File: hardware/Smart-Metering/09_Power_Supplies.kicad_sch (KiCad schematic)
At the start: 36 parts, among them J901 BATTERY_1S, SW901 POWER, U901 BQ24074RGT, U902 TPS63001, U903 TPS61089

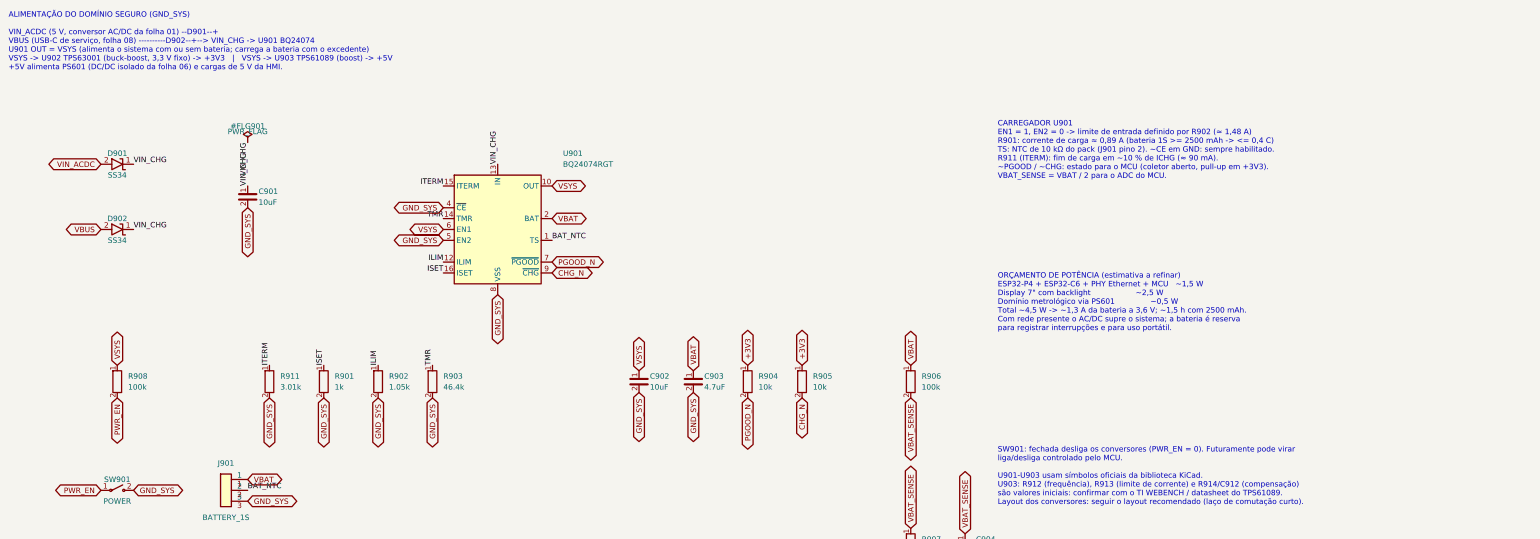
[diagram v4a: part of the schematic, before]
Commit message: Troca o carregador linear BQ24074 pelo chaveado BQ25895
O BQ24074 limitava a entrada a 1,48 A e, com o sistema consumindo cerca
de 5,2 W, sobravam só ~0,3 A para carregar a bateria (mais de 8 h).

09_Power_Supplies:
- U901 BQ25895RTW (símbolo oficial): carregador chaveado com power path
  NVDC; limite de entrada de 2,0 A por R902 (180 Ω), o máximo do
  IRM-10-5; carga de ~0,85 A com a tela ligada;
- D+/D- unidos para detecção como carregador dedicado (DCP);
- divisor do NTC a partir de REGN, L903 2,2 uH, bootstrap, REGN, PMID,
  SYS e BAT conforme o datasheet;
- I2C, ~INT e STAT para o MCU; D901/D902 passam a SS54 (SMC);
- PWR_FLAG em VSYS (pino SYS é passivo no símbolo oficial).

05_Metrology_MCU: PC2 = CHG_INT_N, PB6/PB7 = I2C1 para o carregador.
Documentação de revisão e README atualizados.

Co-Authored-By: Claude Opus 5.5 <noreply@anthropic.com>
Claude-Session: https://claude.ai/code/session_012B8cVkhtjf3eg98UdpNCpf
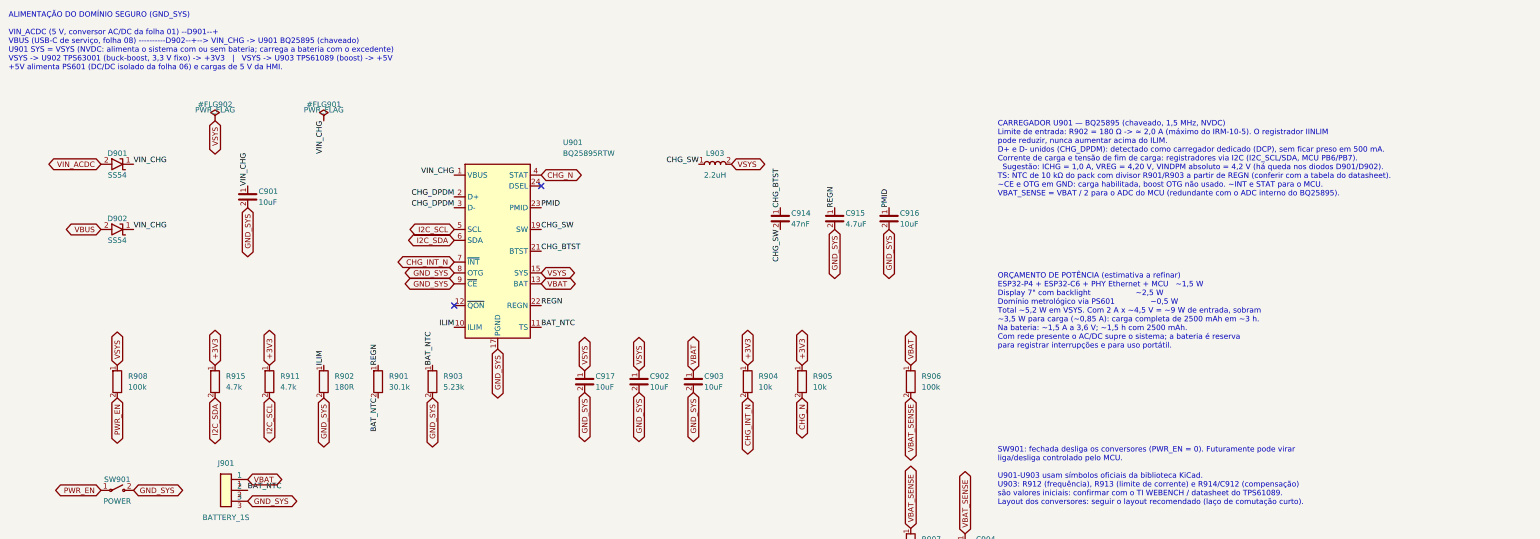
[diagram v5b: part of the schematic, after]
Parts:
- removed U901: BQ24074RGT, Package_DFN_QFN:VQFN-16-1EP_3x3mm_P0.5mm_EP1.6x1.6mm, symbol Battery_Management:BQ24074RGT
- added C914: 47nF, Capacitor_SMD:C_0603_1608Metric, symbol SmartMetering:C_Vert
- added C915: 4.7uF, Capacitor_SMD:C_0805_2012Metric, symbol SmartMetering:C_Vert
- added C916, C917: 10uF, Capacitor_SMD:C_0805_2012Metric, symbol SmartMetering:C_Vert
- added L903: 2.2uH, Inductor_SMD:L_Bourns_SRP7028A_7.3x6.6mm, symbol SmartMetering:L_Horiz
- added R915: 4.7k, Resistor_SMD:R_0603_1608Metric, symbol SmartMetering:R_Vert
- added U901: BQ25895RTW, Package_DFN_QFN:Texas_RTW_WQFN-24-1EP_4x4mm_P0.5mm_EP2.7x2.7mm_ThermalVias, symbol Battery_Management:BQ25895RTW
- C903: value 4.7uF -> 10uF
- D901, D902: value SS34 -> SS54; footprint Diode_SMD:D_SMA -> Diode_SMD:D_SMC
- R901: value 1k -> 30.1k
- R902: value 1.05k -> 180R
- R903: value 46.4k -> 5.23k
- R911: value 3.01k -> 4.7k
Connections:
- net ITERM is gone; now on net +3V3: R911.1
- net TMR is gone; now on net BAT_NTC: R903.1
- net +3V3: now also R915.1
- net BAT_NTC: now also R901.2, U901.11 (TS)
- net CHG_N: now also U901.4 (STAT)
- net GND_SYS: now also C915.2, C916.2, C917.2, U901.17 (PGND), U901.18 (PGND), U901.25 (PGND), U901.8 (OTG), U901.9 (~{CE}); no longer R901.2, R911.2
- net ILIM: now also U901.10 (ILIM)
- net VBAT: now also U901.13 (BAT), U901.14 (BAT)
- net VIN_CHG: now also U901.1 (VBUS)
- net VSYS: now also C917.1, L903.2, U901.15 (SYS), U901.16 (SYS)
- net ISET renamed REGN
- net REGN: now also C915.1, U901.22 (REGN)
- net PGOOD_N renamed CHG_INT_N
- net CHG_INT_N: now also U901.7 (~{INT})
- new net CHG_BTST: C914.1, U901.21 (BTST)
- new net CHG_DPDM: U901.2 (D+), U901.3 (D-)
- new net CHG_SW: C914.2, L903.1, U901.19 (SW), U901.20 (SW)
- new net I2C_SCL: R911.2, U901.5 (SCL)
- new net I2C_SDA: R915.2, U901.6 (SDA)
- new net PMID: C916.1, U901.23 (PMID)
- no-connect marks 0 -> 2
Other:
- note added: "ALIMENTAÇÃO DO DOMÍNIO SEGURO (GND_SYS) VIN_ACDC (5 V, conversor AC/DC da folha 01) --D901--+ VBUS (USB-C de serviço, folha 08) ----------D902--+--> VIN_CHG -> U901 BQ25895 (chaveado) U901 SYS = VSYS (NVDC: alimenta o sistema com ou sem bateria; carrega a bateria com o excedente) VSYS -> U902 TPS63001 (buck-boost, 3,3 V fixo) -> +3V3 | VSYS -> U903 TPS61089 (boost) -> +5V +5V alimenta PS601 (DC/D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"
- note added: "CARREGADOR U901 — BQ25895 (chaveado, 1,5 MHz, NVDC) Limite de entrada: R902 = 180 Ω -> ≈ 2,0 A (máximo do IRM-10-5). O registrador IINLIM pode reduzir, nunca aumentar acima do ILIM. D+ e D- unidos (CHG_DPDM): detectado como carregador dedicado (DCP), sem ficar preso em 500 mA. Corrente de carga e tensão de fim de carga: registradores via I2C (I2C_SCL/SDA, MCU PB6/PB7). Sugestão: ICHG = 1,0 A, VRE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"
- note added: "ORÇAMENTO DE POTÊNCIA (estimativa a refinar) ESP32-P4 + ESP32-C6 + PHY Ethernet + MCU ~1,5 W Display 7" com backlight ~2,5 W Domínio metrológico via PS601 ~0,5 W Total ~5,2 W em VSYS. Com 2 A x ~4,5 V = ~9 W de entrada, sobram ~3,5 W para carga (~0,85 A): carga completa de 2500 mAh em ~3 h. Na bateria: ~1,5 A a 3,6 V; ~1,5 h com 2500 mAh. Com rede presente o AC/DC supre o sistema; a bateria é res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"
- note removed: "ALIMENTAÇÃO DO DOMÍNIO SEGURO (GND_SYS) VIN_ACDC (5 V, conversor AC/DC da folha 01) --D901--+ VBUS (USB-C de serviço, folha 08) ----------D902--+--> VIN_CHG -> U901 BQ24074 U901 OUT = VSYS (alimenta o sistema com ou sem bateria; carrega a bateria com o excedente) VSYS -> U902 TPS63001 (buck-boost, 3,3 V fixo) -> +3V3 | VSYS -> U903 TPS61089 (boost) -> +5V +5V alimenta PS601 (DC/DC isolado da folh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"
- note removed: "CARREGADOR U901 EN1 = 1, EN2 = 0 -> limite de entrada definido por R902 (≈ 1,48 A) R901: corrente de carga ≈ 0,89 A (bateria 1S >= 2500 mAh -> <= 0,4 C) TS: NTC de 10 kΩ do pack (J901 pino 2). ~CE em GND: sempre habilitado. R911 (ITERM): fim de carga em ~10 % de ICHG (≈ 90 mA). ~PGOOD / ~CHG: estado para o MCU (coletor aberto, pull-up em +3V3). VBAT_SENSE = VBAT / 2 para o ADC do MCU."
- note removed: "ORÇAMENTO DE POTÊNCIA (estimativa a refinar) ESP32-P4 + ESP32-C6 + PHY Ethernet + MCU ~1,5 W Display 7" com backlight ~2,5 W Domínio metrológico via PS601 ~0,5 W Total ~4,5 W -> ~1,3 A da bateria a 3,6 V; ~1,5 h com 2500 mAh. Com rede presente o AC/DC supre o sistema; a bateria é reserva para registrar interrupções e para uso portátil."

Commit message: Resolve as pendências da revisão do esquemático
P1  ADE9430: footprint VQFN-40 6x6 com EP de 4,15 mm, compatível com as
    variantes CP-40 de 6x6 mm (EP de 3,9 a 4,7 mm).
P2  Confirmado no datasheet: MISO solto com SS alto (pull-up de 100 kΩ)
    e NC1/NC2 em GND, como já estava.
P3  J301-J304: headers JST PH de 4 vias cabeados até conectores M8
    fêmea de painel (à prova de toque).
P4  PS601 -> U606 ADuM6000 (isoPower 5 kVrms, símbolo oficial).
P5  PS101 -> RAC20-05SK/277 (85-305 VAC, 120-430 VDC, 20 W); fusíveis
    T500mA, R101 3 W, C101 10 uF/450 V; entrada do BQ25895 a 3 A.
P7  TPS61089 -> TPS61022 (compensação interna, sem valores a ajustar).
P8  Placa EV alimentada pelos pinos 5 V do J1 (nota na folha 07).
P9  EEPROM de calibração 24LC64 no I2C1.
P10 Labels globais de uma só folha convertidos em locais.

Verificação: 223 componentes, nenhum pino solto, nenhuma net sem fonte,
nenhum conflito de saída, isolação íntegra, todos os footprints
existentes na biblioteca oficial do KiCad.

Co-Authored-By: Claude Opus 5.5 <noreply@anthropic.com>
Claude-Session: https://claude.ai/code/session_012B8cVkhtjf3eg98UdpNCpf
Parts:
- removed C912: 4.7nF, Capacitor_SMD:C_0603_1608Metric, symbol SmartMetering:C_Vert
- removed C913: 2.2uF, Capacitor_SMD:C_0603_1608Metric, symbol SmartMetering:C_Vert
- removed R912: 301k, Resistor_SMD:R_0603_1608Metric, symbol SmartMetering:R_Vert
- removed R913: 200k, Resistor_SMD:R_0603_1608Metric, symbol SmartMetering:R_Vert
- removed R914: 15k, Resistor_SMD:R_0603_1608Metric, symbol SmartMetering:R_Vert
- removed U903: TPS61089, Package_DFN_QFN:Texas_VQFN-RNR0011A-11, symbol Regulator_Switching:TPS61089
- added U903: TPS61022, Package_DFN_QFN:Texas_RWU0007A_VQFN-7_2x2mm_P0.5mm, symbol Converter_DCDC:TPS61022
- C908: value 10uF -> 22uF; footprint Capacitor_SMD:C_0805_2012Metric -> Capacitor_SMD:C_1206_3216Metric
- C911: value 100nF -> 22uF; footprint Capacitor_SMD:C_0603_1608Metric -> Capacitor_SMD:C_1206_3216Metric
- L902: value 2.2uH -> 1uH
- R902: value 180R -> 120R
- R909: value 316k -> 732k
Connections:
- net BOOT_5V is gone; now on net +5V: C911.1
- net +5V: now also U903.3 (VOUT)
- net FB_5V: now also U903.4 (FB)
- net GND_SYS: now also C911.2, U903.1 (GND)
- net PWR_EN: now also U903.5 (EN)
- net SW_5V: now also U903.2 (SW); no longer C911.2
- net VSYS: now also U903.6 (MODE), U903.7 (VIN)
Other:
- note added: "ALIMENTAÇÃO DO DOMÍNIO SEGURO (GND_SYS) VIN_ACDC (5 V, conversor AC/DC da folha 01) --D901--+ VBUS (USB-C de serviço, folha 08) ----------D902--+--> VIN_CHG -> U901 BQ25895 (chaveado) U901 SYS = VSYS (NVDC: alimenta o sistema com ou sem bateria; carrega a bateria com o excedente) VSYS -> U902 TPS63001 (buck-boost, 3,3 V fixo) -> +3V3 | VSYS -> U903 TPS61022 (boost) -> +5V +5V alimenta PS601 (DC/D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"
- note added: "CARREGADOR U901 — BQ25895 (chaveado, 1,5 MHz, NVDC) Limite de entrada: R902 = 120 Ω -> ≈ 3,0 A (RAC20-05SK fornece 4 A). O registrador IINLIM pode reduzir, nunca aumentar acima do ILIM. D+ e D- unidos (CHG_DPDM): detectado como carregador dedicado (DCP), sem ficar preso em 500 mA. Corrente de carga e tensão de fim de carga: registradores via I2C (I2C_SCL/SDA, MCU PB6/PB7). Sugestão: ICHG = 1,0 A,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"
- note added: "ORÇAMENTO DE POTÊNCIA (estimativa a refinar) ESP32-P4 + ESP32-C6 + PHY Ethernet + MCU ~1,5 W Display 7" com backlight ~2,5 W Domínio metrológico via PS601 ~0,5 W Total ~5,2 W em VSYS. Com 3 A x ~4,5 V = ~13 W de entrada, sobra folga para carga de 1,0 A (definida por firmware): ~2,5 h para 2500 mAh. Na bateria: ~1,5 A a 3,6 V; ~1,5 h com 2500 mAh. Com rede presente o AC/DC supre o sistema; a bater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"
- note added: "SW901: fechada desliga os conversores (PWR_EN = 0). Futuramente pode virar liga/desliga controlado pelo MCU. U901-U903 usam símbolos oficiais da biblioteca KiCad. U903 TPS61022: compensação interna; MODE em VSYS = PWM forçado (menos ruído). Layout dos conversores: seguir o layout recomendado (laço de comutação curto)."
- note removed: "ALIMENTAÇÃO DO DOMÍNIO SEGURO (GND_SYS) VIN_ACDC (5 V, conversor AC/DC da folha 01) --D901--+ VBUS (USB-C de serviço, folha 08) ----------D902--+--> VIN_CHG -> U901 BQ25895 (chaveado) U901 SYS = VSYS (NVDC: alimenta o sistema com ou sem bateria; carrega a bateria com o excedente) VSYS -> U902 TPS63001 (buck-boost, 3,3 V fixo) -> +3V3 | VSYS -> U903 TPS61089 (boost) -> +5V +5V alimenta PS601 (DC/D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"
- note removed: "CARREGADOR U901 — BQ25895 (chaveado, 1,5 MHz, NVDC) Limite de entrada: R902 = 180 Ω -> ≈ 2,0 A (máximo do IRM-10-5). O registrador IINLIM pode reduzir, nunca aumentar acima do ILIM. D+ e D- unidos (CHG_DPDM): detectado como carregador dedicado (DCP), sem ficar preso em 500 mA. Corrente de carga e tensão de fim de carga: registradores via I2C (I2C_SCL/SDA, MCU PB6/PB7). Sugestão: ICHG = 1,0 A, VRE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"
- note removed: "ORÇAMENTO DE POTÊNCIA (estimativa a refinar) ESP32-P4 + ESP32-C6 + PHY Ethernet + MCU ~1,5 W Display 7" com backlight ~2,5 W Domínio metrológico via PS601 ~0,5 W Total ~5,2 W em VSYS. Com 2 A x ~4,5 V = ~9 W de entrada, sobram ~3,5 W para carga (~0,85 A): carga completa de 2500 mAh em ~3 h. Na bateria: ~1,5 A a 3,6 V; ~1,5 h com 2500 mAh. Com rede presente o AC/DC supre o sistema; a bateria é res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"
- note removed: "SW901: fechada desliga os conversores (PWR_EN = 0). Futuramente pode virar liga/desliga controlado pelo MCU. U901-U903 usam símbolos oficiais da biblioteca KiCad. U903: R912 (frequência), R913 (limite de corrente) e R914/C912 (compensação) são valores iniciais: confirmar com o TI WEBENCH / datasheet do TPS61089. Layout dos conversores: seguir o layout recomendado (laço de comutação curto)."

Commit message: Corrige os achados da revisão automática do PR #1
- BQ25895: divisor do TS invertido (R901 = 5,23 kΩ REGN-TS, R903 = 30,1 kΩ
  TS-GND); antes o carregador via sobretemperatura e não carregava.
- Detecção da fonte: Q902 une D+/D- (DCP, 3 A) só com o AC/DC presente;
  só pelo USB-C a entrada fica em 500 mA. Q901 corta o VBUS quando o AC/DC
  está presente (prioridade do AC/DC sobre a porta USB). R912 polariza os dois.
- DRC: classes DIVIDER_A/B/C, regras entre divisores de fases diferentes
  (3,0 mm), divisor x domínio metrológico (2,0 mm), divisor x rede de outras
  fases (3,0 mm), barramento HV com clearance e creepage, creepage da
  barreira 8,0 mm (com regra própria entre as fileiras dos isoladores).
- Pinos sem uso do lado isolado do U606 classificados no domínio quente.
- Projeto KiCad: folha raiz correta em top_level_sheets.
- PCB: Q901, Q902, R912 posicionados; C103 afastado dos pads quentes de
  U602/U606; zonas com margem para 8 mm na barreira.
- Documentação: ISO7762/ISO7761 na arquitetura, limite de entrada de 3 A
  na revisão, roteamento do domínio quente descrito como parcial.

Co-Authored-By: Claude Opus 5.5 <noreply@anthropic.com>
Claude-Session: https://claude.ai/code/session_012B8cVkhtjf3eg98UdpNCpf
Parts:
- added Q901: AO3401A, Package_TO_SOT_SMD:SOT-23, symbol Transistor_FET:AO3401A
- added Q902: 2N7002, Package_TO_SOT_SMD:SOT-23, symbol Transistor_FET:2N7002
- added R912: 100k, Resistor_SMD:R_0603_1608Metric, symbol SmartMetering:R_Vert
- R901: value 30.1k -> 5.23k
- R903: value 5.23k -> 30.1k
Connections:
- net GND_SYS: now also R912.2
- net VBUS: now also Q901.2 (S); no longer D902.2 (A)
- net VIN_ACDC: now also Q901.1 (G), Q902.1 (G), R912.1
- net CHG_DPDM renamed CHG_DM
- net CHG_DM: now also Q902.2 (S); no longer U901.2 (D+)
- new net CHG_DP: Q902.3 (D), U901.2 (D+)
- new net VBUS_SW: D902.2 (A), Q901.3 (D)
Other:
- note added: "ALIMENTAÇÃO DO DOMÍNIO SEGURO (GND_SYS) VIN_ACDC (5 V, conversor AC/DC da folha 01) --D901--+ VBUS (USB-C de serviço, folha 08) --Q901--D902--+--> VIN_CHG -> U901 BQ25895 (chaveado) Q901 corta o VBUS quando o AC/DC está presente: a porta USB nunca supre a placa junto com o AC/DC. U901 SYS = VSYS (NVDC: alimenta o sistema com ou sem bateria; carrega a bateria com o excedente) VSYS -> U902 TPS63001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"
- note added: "CARREGADOR U901 — BQ25895 (chaveado, 1,5 MHz, NVDC) Limite de entrada: R902 = 120 Ω -> ≈ 3,0 A (RAC20-05SK fornece 4 A). O registrador IINLIM pode reduzir, nunca aumentar acima do ILIM. D+/D- do BQ25895: Q902 os une só com o AC/DC presente (DCP -> 3 A, limitado pelo ILIM). Só pelo USB-C: D+/D- soltos -> detecção SDP/desconhecida -> 500 mA (não sobrecarrega a porta do PC). Corrente de carga e tens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"
- note removed: "ALIMENTAÇÃO DO DOMÍNIO SEGURO (GND_SYS) VIN_ACDC (5 V, conversor AC/DC da folha 01) --D901--+ VBUS (USB-C de serviço, folha 08) ----------D902--+--> VIN_CHG -> U901 BQ25895 (chaveado) U901 SYS = VSYS (NVDC: alimenta o sistema com ou sem bateria; carrega a bateria com o excedente) VSYS -> U902 TPS63001 (buck-boost, 3,3 V fixo) -> +3V3 | VSYS -> U903 TPS61022 (boost) -> +5V +5V alimenta PS601 (DC/D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"
- note removed: "CARREGADOR U901 — BQ25895 (chaveado, 1,5 MHz, NVDC) Limite de entrada: R902 = 120 Ω -> ≈ 3,0 A (RAC20-05SK fornece 4 A). O registrador IINLIM pode reduzir, nunca aumentar acima do ILIM. D+ e D- unidos (CHG_DPDM): detectado como carregador dedicado (DCP), sem ficar preso em 500 mA. Corrente de carga e tensão de fim de carga: registradores via I2C (I2C_SCL/SDA, MCU PB6/PB7). Sugestão: ICHG = 1,0 A,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"
